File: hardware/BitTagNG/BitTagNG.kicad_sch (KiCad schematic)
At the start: 22 parts, among them Q501 Q_NPN_BEC, U1 at25ex321D-UUN, U2 adxl367, U302 stm32l431kc, U501 RV-3028-C7

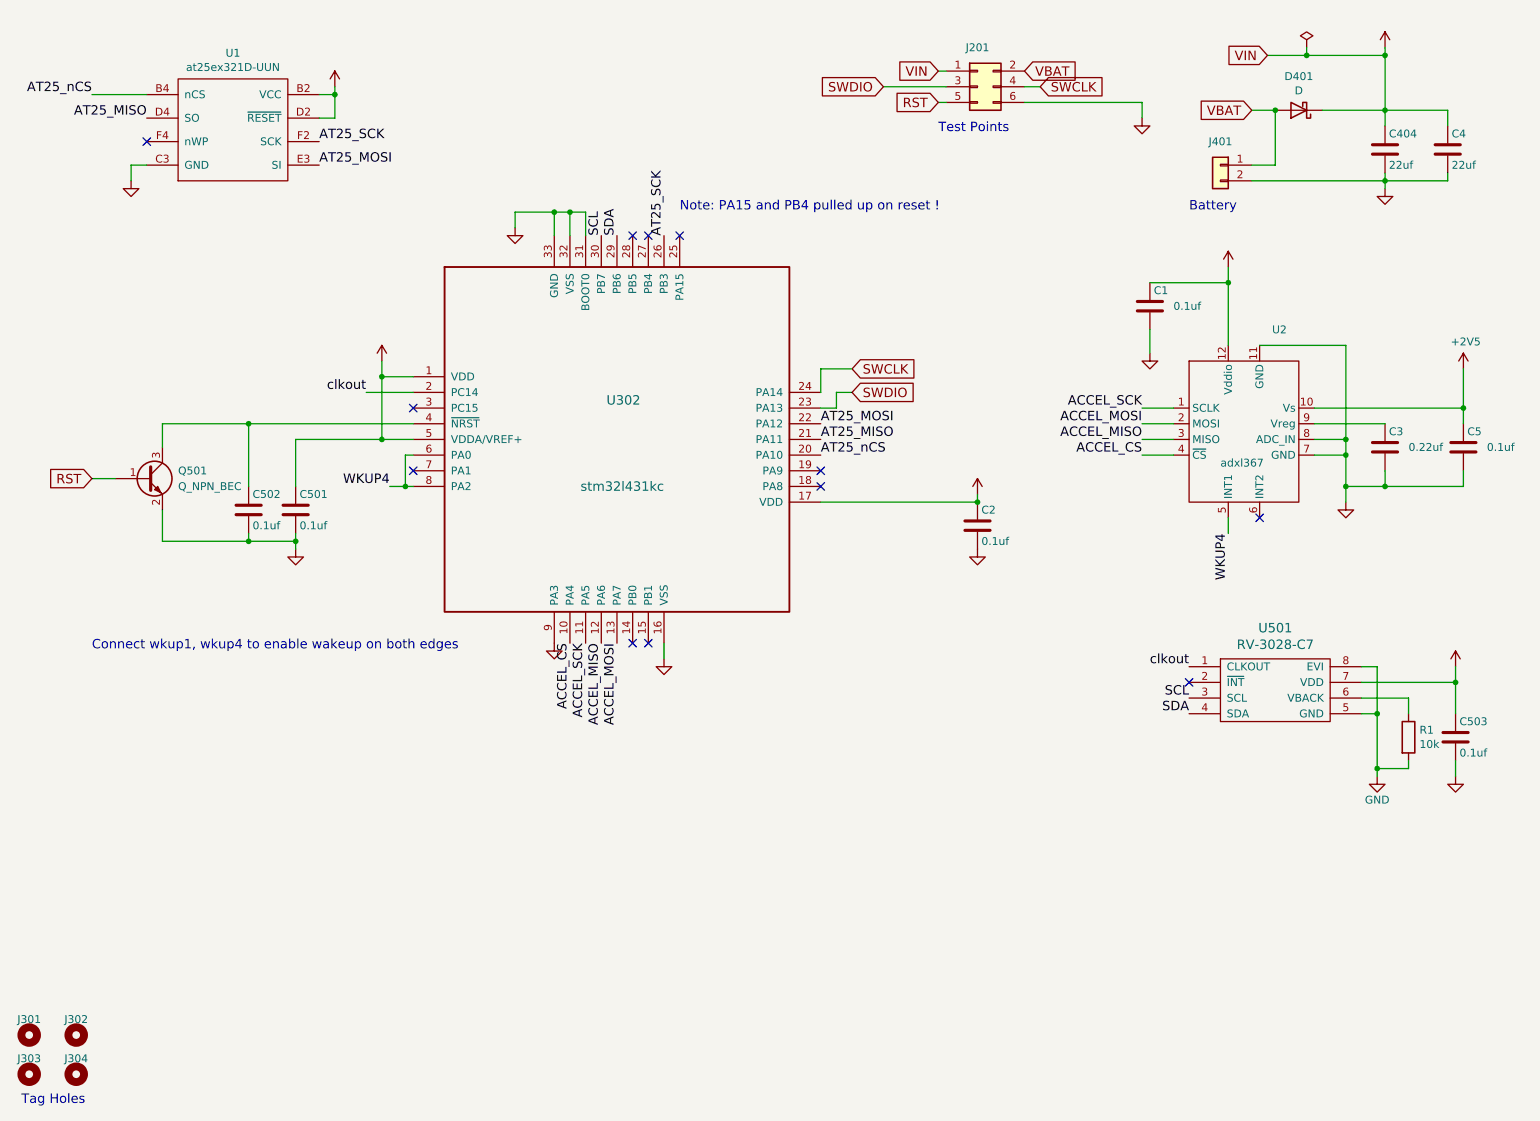
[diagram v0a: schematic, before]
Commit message: update parts in BitTagNG
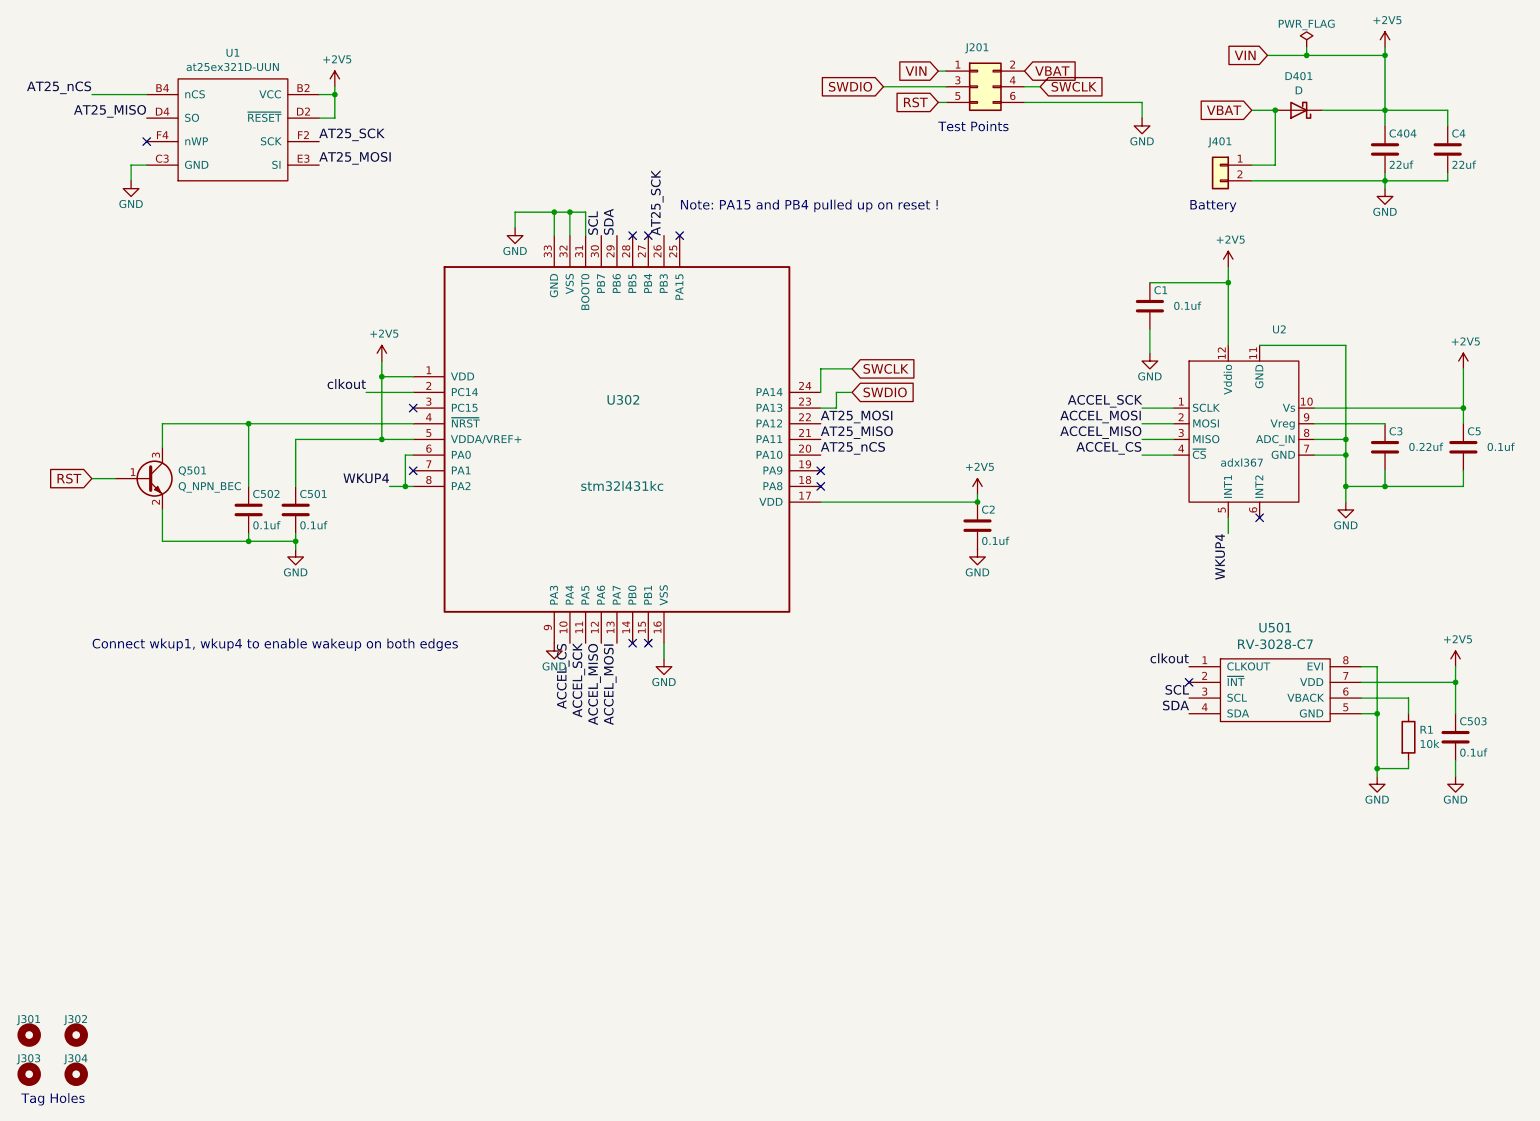
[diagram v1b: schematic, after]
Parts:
- C1, C2, C5, C501, C502, C503: LCSC (none) -> C181047
- C3: DISTPN 490-10392-1-ND -> 490-GRM033R61E224ME01DCT-ND; LCSC (none) -> C710823; MPN GRM033C80J224KE90D -> GRM033R61E224ME01D
- C4, C404: LCSC (none) -> C2179118
- D401: LCSC (none) -> C2886012
- J201: value (none) -> CONN_02X04; footprint (none) -> AccelTag:tagpoints6; now left out of the parts list
- J301, J302, J303, J304: value (none) -> Conn_01x01; footprint (none) -> AccelTag:taghole1.1mm; now left out of the parts list
- J401: value (none) -> CONN_01X02; footprint (none) -> AccelTag:MS621; now left out of the parts list
- Q501: LCSC (none) -> C686658
- R1: LCSC (none) -> C106225
- U1: DISTPN 1265-AT25XE321D-UUN-TCT-ND -> 724-AT25FF321A-UUN-T; LCSC (none) -> C1858339; MPN AT25XE321D-UUN-T -> AT25FF321A-UUN-T
- U2: DISTPN (none) -> 584-ADXL367BCCZ-RL7; MFN (none) -> Analog Devices; MPN (none) -> ADXL367BCCZ-RL7
- U302: LCSC (none) -> C1337280
- U501: LCSC (none) -> C3019759

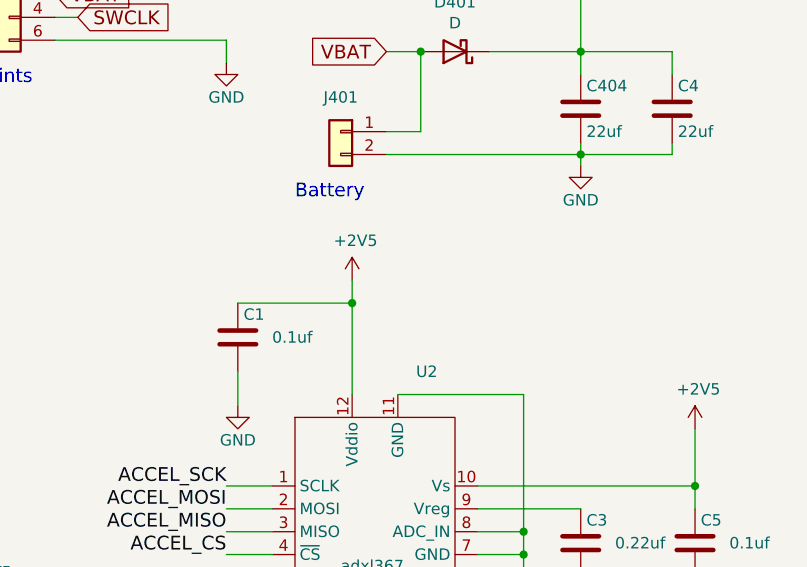
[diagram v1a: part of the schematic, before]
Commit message: update decoupling for adxl367
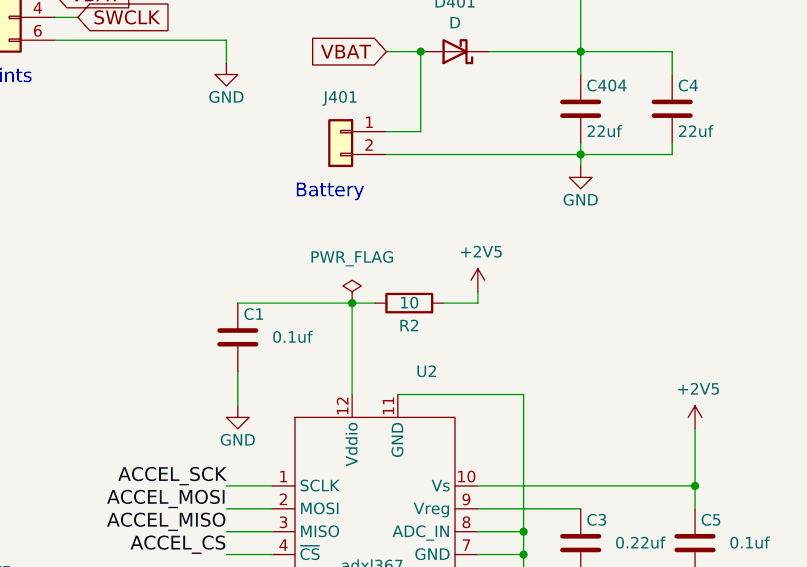
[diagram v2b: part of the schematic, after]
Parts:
- added R2: 10, Resistor_SMD:R_0201_0603Metric, symbol Device:R
- U501: footprint RV-8803-C7 -> AccelTag:RV-8803-C7
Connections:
- net +2V5: now also R2.2; no longer C1.1, U2.12 (Vddio)
- new net: C1.1, R2.1, U2.12 (Vddio)
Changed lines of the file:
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@@
+    (stroke (width 0) (type default) (color 0 0 0 0))
+  )
+  (wire (pts (xy 233.68 59.69) (xy 233.68 60.96))
     (stroke (width 0) (type default) (color 0 0 0 0))
   )
@@
     (stroke (width 0) (type default) (color 0 0 0 0))
   )
+  (wire (pts (xy 219.71 60.96) (xy 222.25 60.96))
+    (stroke (width 0) (type default) (color 0 0 0 0))
+  )
   (wire (pts (xy 241.3 128.27) (xy 248.92 128.27))
     (stroke (width 0) (type default) (color 0 0 0 0))
@@
     (stroke (width 0) (type default) (color 0 0 0 0))
   )
+  (wire (pts (xy 233.68 60.96) (xy 229.87 60.96))
+    (stroke (width 0) (type default) (color 0 0 0 0))
+  )
   (wire (pts (xy 226.06 24.13) (xy 232.41 24.13))
     (stroke (width 0) (type default) (color 0 0 0 0))
@@
   )
   (wire (pts (xy 223.52 44.45) (xy 245.11 44.45))
-    (stroke (width 0) (type default) (color 0 0 0 0))
-  )
-  (wire (pts (xy 219.71 60.96) (xy 219.71 58.42))
     (stroke (width 0) (type default) (color 0 0 0 0))
   )
@@
       (effects (font (size 1.524 1.524)))
     )
-    (property "Footprint" "RV-8803-C7" (id 2) (at 224.79 115.57 0)
+    (property "Footprint" "AccelTag:RV-8803-C7" (id 2) (at 224.79 115.57 0)
       (effects (font (size 1.524 1.524)) hide)
     )
@@
     (pin "1")
   )
-  (symbol (lib_id "power:+2V5") (at 219.71 58.42 0) (unit 1)
-    (in_bom yes) (on_board yes)
-    (property "Reference" "#PWR0104" (id 0) (at 219.71 62.23 0)
-      (effects (font (size 1.27 1.27)) hide)
-    )
-    (property "Value" "+2V5" (id 1) (at 220.091 54.0258 0))
-    (property "Footprint" "" (id 2) (at 219.71 58.42 0)
-      (effects (font (size 1.27 1.27)) hide)
-    )
-    (property "Datasheet" "" (id 3) (at 219.71 58.42 0)
-      (effects (font (size 1.27 1.27)) hide)
-    )
-    (pin "1")
-  )
   (symbol (lib_id "power:GND") (at 238.76 96.52 0) (unit 1)
     (in_bom yes) (on_board yes)
@@
     (pin "1")
   )
+  (symbol (lib_id "power:PWR_FLAG") (at 219.71 60.96 0) (unit 1)
+    (in_bom yes) (on_board yes) (fields_autoplaced)
+    (property "Reference" "#FLG0101" (id 0) (at 219.71 59.055 0)
+      (effects (font (size 1.27 1.27)) hide)
+    )
+    (property "Value" "PWR_FLAG" (id 1) (at 219.71 55.88 0))
+    (property "Footprint" "" (id 2) (at 219.71 60.96 0)
+      (effects (font (size 1.27 1.27)) hide)
+    )
+    (property "Datasheet" "~" (id 3) (at 219.71 60.96 0)
+      (effects (font (size 1.27 1.27)) hide)
+    )
+    (pin "1")
+  )
   (symbol (lib_id "power:+2V5") (at 257.81 74.93 0) (unit 1)
     (in_bom yes) (on_board yes)
@@
     )
     (pin "1")
+  )
+  (symbol (lib_id "power:+2V5") (at 233.68 59.69 0) (unit 1)
+    (in_bom yes) (on_board yes)
+    (property "Reference" "#PWR0104" (id 0) (at 233.68 63.5 0)
+      (effects (font (size 1.27 1.27)) hide)
+    )
+    (property "Value" "+2V5" (id 1) (at 234.061 55.2958 0))
+    (property "Footprint" "" (id 2) (at 233.68 59.69 0)
+      (effects (font (size 1.27 1.27)) hide)
+    )
+    (property "Datasheet" "" (id 3) (at 233.68 59.69 0)
+      (effects (font (size 1.27 1.27)) hide)
+    )
+    (pin "1")
+  )
+  (symbol (lib_id "Device:R") (at 226.06 60.96 90) (unit 1)
+    (in_bom yes) (on_board yes)
+    (property "Reference" "R2" (id 0) (at 226.06 63.5 90))
+    (property "Value" "10" (id 1) (at 226.06 60.96 90))
+    (property "Footprint" "Resistor_SMD:R_0201_0603Metric" (id 2) (at 226.06 62.738 90)
+      (effects (font (size 1.27 1.27)) hide)
+    )
+    (property "Datasheet" "~" (id 3) (at 226.06 60.96 0)
+      (effects (font (size 1.27 1.27)) hide)
+    )
+    (pin "1")
+    (pin "2")
   )
   (symbol (lib_id "power:GND") (at 243.84 140.97 0) (unit 1)
@@
   )
   (symbol_instances
+    (path "/1c7957a0-bd0d-4961-b213-b0c8bb378155"
+      (reference "#FLG0101") (unit 1) (value "PWR_FLAG") (footprint "")
+    )
     (path "/00000000-0000-0000-0000-00005c0f14f0"
       (reference "#FLG0102") (unit 1) (value "PWR_FLAG") (footprint "")
@@
       (reference "#PWR0103") (unit 1) (value "GND") (footprint "")
     )
-    (path "/00000000-0000-0000-0000-00006104d732"
+    (path "/58b6b2f1-311e-47a4-830d-be1459c8432d"
       (reference "#PWR0104") (unit 1) (value "+2V5") (footprint "")
     )
@@
       (reference "R1") (unit 1) (value "10k") (footprint "Resistor_SMD:R_0201_0603Metric")
     )
+    (path "/7666a996-c746-4ba9-85d0-dff249c3b2d0"
+      (reference "R2") (unit 1) (value "10") (footprint "Resistor_SMD:R_0201_0603Metric")
+    )
     (path "/00000000-0000-0000-0000-00005fd47223"
       (reference "U1") (unit 1) (value "at25ex321D-UUN") (footprint "AccelTag:adesto_wlcsp12")
@@
     )
     (path "/00000000-0000-0000-0000-00005ef60ddb"
-      (reference "U501") (unit 1) (value "RV-3028-C7") (footprint "RV-8803-C7")
-    )
-  )
+      (reference "U501") (unit 1) (value "RV-3028-C7") (footprint "AccelTag:RV-8803-C7")
+    )
+  )

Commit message: update bittagng
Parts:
- removed R2: 10, Resistor_SMD:R_0201_0603Metric, symbol Device:R
- C1, C2, C5, C501, C502, C503: MPN GRM033C81E104KE14D -> C181047; Macrofab MF-CAP-0402-0.1uF -> (none)
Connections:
- net +2V5: now also C1.1, U2.12 (Vddio)
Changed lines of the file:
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@@
-    (stroke (width 0) (type default) (color 0 0 0 0))
-  )
-  (wire (pts (xy 233.68 59.69) (xy 233.68 60.96))
     (stroke (width 0) (type default) (color 0 0 0 0))
   )
@@
     (stroke (width 0) (type default) (color 0 0 0 0))
   )
-  (wire (pts (xy 219.71 60.96) (xy 222.25 60.96))
-    (stroke (width 0) (type default) (color 0 0 0 0))
-  )
   (wire (pts (xy 241.3 128.27) (xy 248.92 128.27))
     (stroke (width 0) (type default) (color 0 0 0 0))
@@
   )
   (wire (pts (xy 256.54 125.73) (xy 256.54 130.81))
-    (stroke (width 0) (type default) (color 0 0 0 0))
-  )
-  (wire (pts (xy 233.68 60.96) (xy 229.87 60.96))
     (stroke (width 0) (type default) (color 0 0 0 0))
   )
@@
       (effects (font (size 1.27 1.27)) hide)
     )
-    (property "Macrofab" "MF-CAP-0402-0.1uF" (id 4) (at 60.96 97.79 0)
+    (property "Macrofab" "" (id 4) (at 60.96 97.79 0)
       (effects (font (size 1.524 1.524)) hide)
     )
@@
       (effects (font (size 1.524 1.524)) hide)
     )
-    (property "MPN" "GRM033C81E104KE14D" (id 6) (at 60.96 97.79 0)
+    (property "MPN" "C181047" (id 6) (at 60.96 97.79 0)
       (effects (font (size 1.524 1.524)) hide)
     )
@@
       (effects (font (size 1.27 1.27)) hide)
     )
-    (property "Macrofab" "MF-CAP-0402-0.1uF" (id 4) (at 68.58 97.79 0)
+    (property "Macrofab" "" (id 4) (at 68.58 97.79 0)
       (effects (font (size 1.524 1.524)) hide)
     )
@@
       (effects (font (size 1.524 1.524)) hide)
     )
-    (property "MPN" "GRM033C81E104KE14D" (id 6) (at 68.58 97.79 0)
+    (property "MPN" "C181047" (id 6) (at 68.58 97.79 0)
       (effects (font (size 1.524 1.524)) hide)
     )
@@
       (effects (font (size 1.524 1.524)) hide)
     )
-    (property "MPN" "GRM033C81E104KE14D" (id 5) (at 256.54 134.62 0)
+    (property "MPN" "C181047" (id 5) (at 256.54 134.62 0)
       (effects (font (size 1.524 1.524)) hide)
     )
@@
       (effects (font (size 1.27 1.27)) hide)
     )
-    (property "Macrofab" "MF-CAP-0402-0.1uF" (id 7) (at 168.91 297.18 0)
+    (property "Macrofab" "" (id 7) (at 168.91 297.18 0)
       (effects (font (size 1.27 1.27)) hide)
     )
@@
       (effects (font (size 1.27 1.27)) hide)
     )
-    (property "Macrofab" "MF-CAP-0402-0.1uF" (id 4) (at 207.01 64.77 0)
+    (property "Macrofab" "" (id 4) (at 207.01 64.77 0)
       (effects (font (size 1.524 1.524)) hide)
     )
@@
       (effects (font (size 1.27 1.27)) hide)
     )
-    (property "MPN" "GRM033C81E104KE14D" (id 7) (at 29.21 167.64 0)
+    (property "MPN" "C181047" (id 7) (at 29.21 167.64 0)
       (effects (font (size 1.27 1.27)) hide)
     )
@@
       (effects (font (size 1.27 1.27)) hide)
     )
-    (property "Macrofab" "MF-CAP-0402-0.1uF" (id 4) (at 179.07 100.33 0)
+    (property "Macrofab" "" (id 4) (at 179.07 100.33 0)
       (effects (font (size 1.524 1.524)) hide)
     )
@@
       (effects (font (size 1.524 1.524)) hide)
     )
-    (property "MPN" "GRM033C81E104KE14D" (id 6) (at 179.07 100.33 0)
+    (property "MPN" "C181047" (id 6) (at 179.07 100.33 0)
       (effects (font (size 1.524 1.524)) hide)
     )
@@
     (pin "1")
   )
-  (symbol (lib_id "power:PWR_FLAG") (at 219.71 60.96 0) (unit 1)
-    (in_bom yes) (on_board yes) (fields_autoplaced)
-    (property "Reference" "#FLG0101" (id 0) (at 219.71 59.055 0)
-      (effects (font (size 1.27 1.27)) hide)
-    )
-    (property "Value" "PWR_FLAG" (id 1) (at 219.71 55.88 0))
-    (property "Footprint" "" (id 2) (at 219.71 60.96 0)
-      (effects (font (size 1.27 1.27)) hide)
-    )
-    (property "Datasheet" "~" (id 3) (at 219.71 60.96 0)
-      (effects (font (size 1.27 1.27)) hide)
-    )
-    (pin "1")
-  )
   (symbol (lib_id "power:+2V5") (at 257.81 74.93 0) (unit 1)
     (in_bom yes) (on_board yes)
@@
     (pin "1")
   )
-  (symbol (lib_id "power:+2V5") (at 233.68 59.69 0) (unit 1)
-    (in_bom yes) (on_board yes)
-    (property "Reference" "#PWR0104" (id 0) (at 233.68 63.5 0)
-      (effects (font (size 1.27 1.27)) hide)
-    )
-    (property "Value" "+2V5" (id 1) (at 234.061 55.2958 0))
-    (property "Footprint" "" (id 2) (at 233.68 59.69 0)
-      (effects (font (size 1.27 1.27)) hide)
-    )
-    (property "Datasheet" "" (id 3) (at 233.68 59.69 0)
-      (effects (font (size 1.27 1.27)) hide)
-    )
-    (pin "1")
-  )
-  (symbol (lib_id "Device:R") (at 226.06 60.96 90) (unit 1)
-    (in_bom yes) (on_board yes)
-    (property "Reference" "R2" (id 0) (at 226.06 63.5 90))
-    (property "Value" "10" (id 1) (at 226.06 60.96 90))
-    (property "Footprint" "Resistor_SMD:R_0201_0603Metric" (id 2) (at 226.06 62.738 90)
-      (effects (font (size 1.27 1.27)) hide)
-    )
-    (property "Datasheet" "~" (id 3) (at 226.06 60.96 0)
-      (effects (font (size 1.27 1.27)) hide)
-    )
-    (pin "1")
-    (pin "2")
+  (symbol (lib_id "power:+2V5") (at 219.71 60.96 0) (unit 1)
+    (in_bom yes) (on_board yes)
+    (property "Reference" "#PWR0104" (id 0) (at 219.71 64.77 0)
+      (effects (font (size 1.27 1.27)) hide)
+    )
+    (property "Value" "+2V5" (id 1) (at 220.091 56.5658 0))
+    (property "Footprint" "" (id 2) (at 219.71 60.96 0)
+      (effects (font (size 1.27 1.27)) hide)
+    )
+    (property "Datasheet" "" (id 3) (at 219.71 60.96 0)
+      (effects (font (size 1.27 1.27)) hide)
+    )
+    (pin "1")
   )
   (symbol (lib_id "power:GND") (at 243.84 140.97 0) (unit 1)
@@
       (effects (font (size 1.27 1.27)) hide)
     )
-    (property "Macrofab" "MF-CAP-0402-0.1uF" (id 4) (at 257.81 87.63 0)
-      (effects (font (size 1.524 1.524)) hide)
-    )
     (property "MFN" "Murata" (id 5) (at 257.81 87.63 0)
       (effects (font (size 1.524 1.524)) hide)
@@
       (effects (font (size 1.27 1.27)) hide)
     )
-    (property "MPN" "GRM033C81E104KE14D" (id 7) (at 80.01 190.5 0)
+    (property "MPN" "C181047" (id 7) (at 80.01 190.5 0)
       (effects (font (size 1.27 1.27)) hide)
     )
@@
   )
   (symbol_instances
-    (path "/1c7957a0-bd0d-4961-b213-b0c8bb378155"
-      (reference "#FLG0101") (unit 1) (value "PWR_FLAG") (footprint "")
-    )
     (path "/00000000-0000-0000-0000-00005c0f14f0"
       (reference "#FLG0102") (unit 1) (value "PWR_FLAG") (footprint "")
@@
       (reference "R1") (unit 1) (value "10k") (footprint "Resistor_SMD:R_0201_0603Metric")
     )
-    (path "/7666a996-c746-4ba9-85d0-dff249c3b2d0"
-      (reference "R2") (unit 1) (value "10") (footprint "Resistor_SMD:R_0201_0603Metric")
-    )
     (path "/00000000-0000-0000-0000-00005fd47223"
